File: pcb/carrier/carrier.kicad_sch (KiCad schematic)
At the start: 42 parts, among them J1 Freeze footswitch, J2 Clear footswitch, J3 In L / Mono, J4 In R (normalled from In L), J5 Out L / Mono, J6 Out R (ring = plug detect), SW1 Single / Multi, SW2 +5 up / down, U1 Daisy Seed

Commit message: Carrier board: routed, DRC clean, fab outputs
route_pcb.py sets design rules, autoroutes with Freerouting (retrying
until complete), imports the session file, and pours AGND on both
layers; DRC reports 0 violations and 0 unconnected pads. make_fab.py
writes Gerbers, drill files, a zip, and JLC-style BOM and placement
files for the 21 top-side SMD parts.

Pot mounting tabs are now plated (solderable). The jack footprint is a
project copy with its outline on the fab layer, since the jack noses
overhang the rear edge by design.

Co-Authored-By: Claude Opus 5.5 <noreply@anthropic.com>
Claude-Session: https://claude.ai/code/session_01JAavHVgiwWaG4iqEz4KA1Q
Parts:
- J3, J4, J5, J6: footprint Connector_Audio:Jack_6.35mm_Neutrik_NMJ6HCD2_Horizontal -> carrier:Jack_6.35mm_Neutrik_NMJ6HCD2_Horizontal_FabOnlySilk
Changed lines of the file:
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@@
     (property "Reference" "J3" (at 330 35 0) (effects (font (size 1.27 1.27))))
     (property "Value" "In L / Mono" (at 330 55 0) (effects (font (size 1.27 1.27))))
-    (property "Footprint" "Connector_Audio:Jack_6.35mm_Neutrik_NMJ6HCD2_Horizontal" (at 330 45 0) (effects (font (size 1.27 1.27)) hide))
+    (property "Footprint" "carrier:Jack_6.35mm_Neutrik_NMJ6HCD2_Horizontal_FabOnlySilk" (at 330 45 0) (effects (font (size 1.27 1.27)) hide))
     (property "Datasheet" "" (at 330 45 0) (effects (font (size 1.27 1.27)) hide))
     (property "MPN" "Neutrik NMJ6HCD2" (at 330 45 0) (effects (font (size 1.27 1.27)) hide))
@@
     (property "Reference" "J4" (at 330 73 0) (effects (font (size 1.27 1.27))))
     (property "Value" "In R (normalled from In L)" (at 330 93 0) (effects (font (size 1.27 1.27))))
-    (property "Footprint" "Connector_Audio:Jack_6.35mm_Neutrik_NMJ6HCD2_Horizontal" (at 330 83 0) (effects (font (size 1.27 1.27)) hide))
+    (property "Footprint" "carrier:Jack_6.35mm_Neutrik_NMJ6HCD2_Horizontal_FabOnlySilk" (at 330 83 0) (effects (font (size 1.27 1.27)) hide))
     (property "Datasheet" "" (at 330 83 0) (effects (font (size 1.27 1.27)) hide))
     (property "MPN" "Neutrik NMJ6HCD2" (at 330 83 0) (effects (font (size 1.27 1.27)) hide))
@@
     (property "Reference" "J5" (at 330 111 0) (effects (font (size 1.27 1.27))))
     (property "Value" "Out L / Mono" (at 330 131 0) (effects (font (size 1.27 1.27))))
-    (property "Footprint" "Connector_Audio:Jack_6.35mm_Neutrik_NMJ6HCD2_Horizontal" (at 330 121 0) (effects (font (size 1.27 1.27)) hide))
+    (property "Footprint" "carrier:Jack_6.35mm_Neutrik_NMJ6HCD2_Horizontal_FabOnlySilk" (at 330 121 0) (effects (font (size 1.27 1.27)) hide))
     (property "Datasheet" "" (at 330 121 0) (effects (font (size 1.27 1.27)) hide))
     (property "MPN" "Neutrik NMJ6HCD2" (at 330 121 0) (effects (font (size 1.27 1.27)) hide))
@@
     (property "Reference" "J6" (at 330 149 0) (effects (font (size 1.27 1.27))))
     (property "Value" "Out R (ring = plug detect)" (at 330 169 0) (effects (font (size 1.27 1.27))))
-    (property "Footprint" "Connector_Audio:Jack_6.35mm_Neutrik_NMJ6HCD2_Horizontal" (at 330 159 0) (effects (font (size 1.27 1.27)) hide))
+    (property "Footprint" "carrier:Jack_6.35mm_Neutrik_NMJ6HCD2_Horizontal_FabOnlySilk" (at 330 159 0) (effects (font (size 1.27 1.27)) hide))
     (property "Datasheet" "" (at 330 159 0) (effects (font (size 1.27 1.27)) hide))
     (property "MPN" "Neutrik NMJ6HCD2" (at 330 159 0) (effects (font (size 1.27 1.27)) hide))

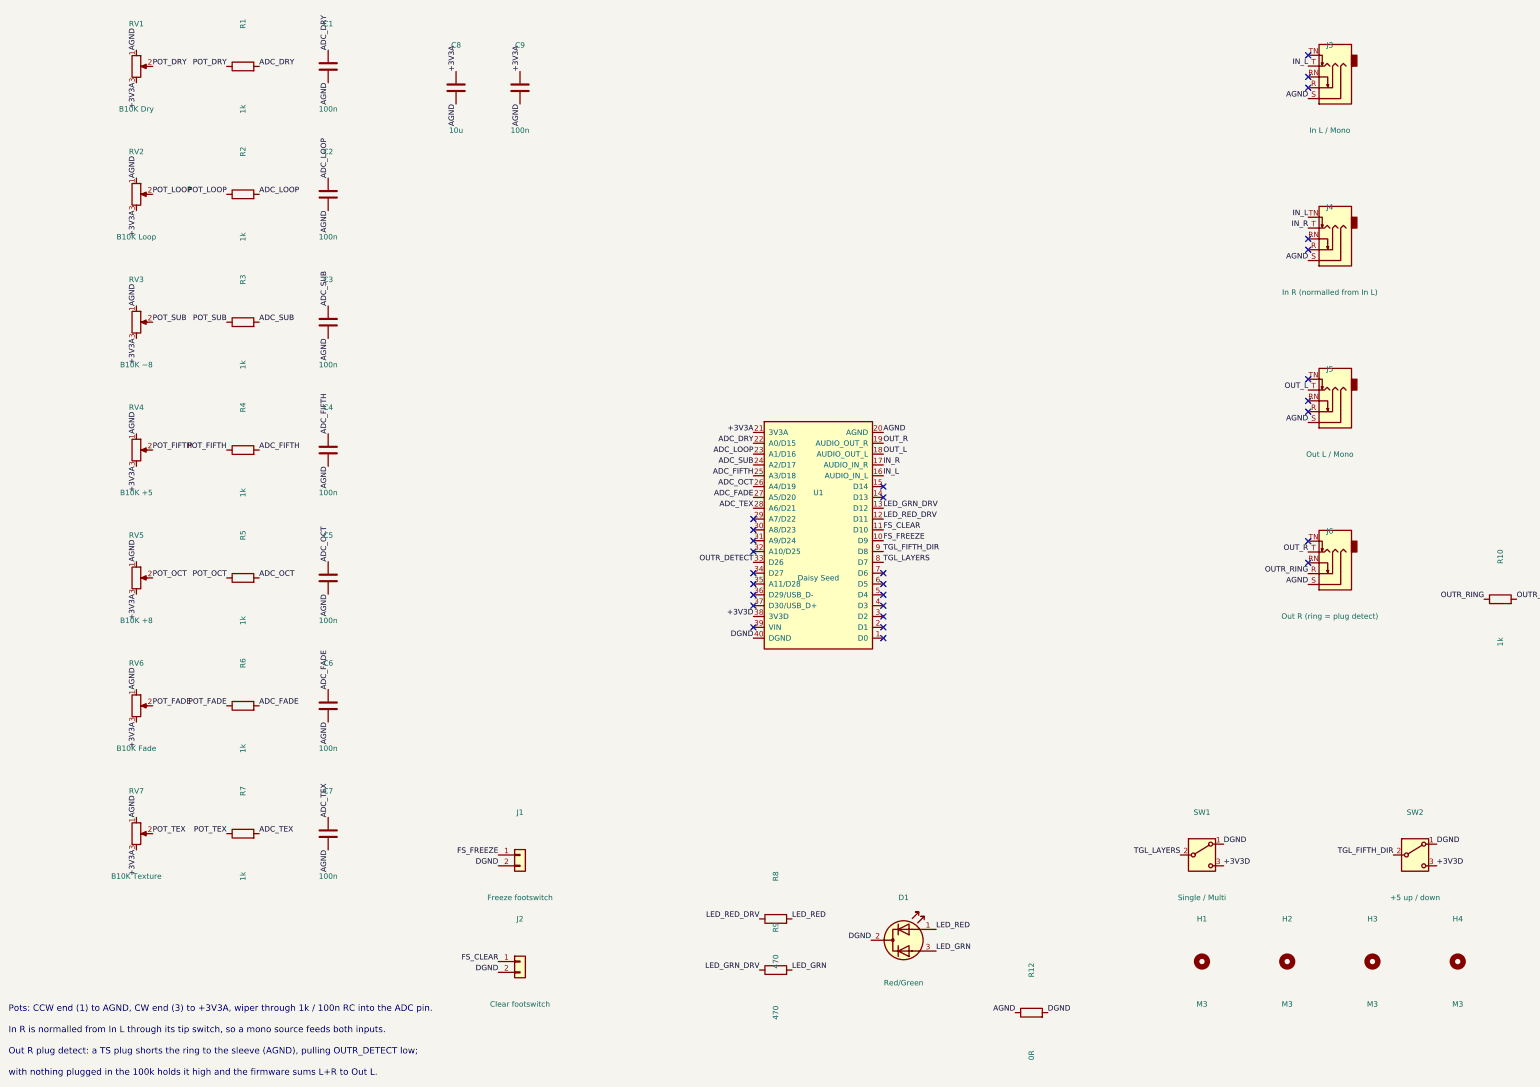
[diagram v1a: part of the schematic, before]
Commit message: Carrier: single ground pour, verified parts
AGND and DGND now tie to one carrier ground (R12 removed), poured on both
layers and stitched with a via grid; re-routed, DRC 0 violations and 0
unconnected. SMD parts carry manufacturer part numbers checked against
their JLC part pages. README records the jack panel-thickness check
(NMJ6HCD2 is rated under 4.7 mm) and the placement-rotation note.

Co-Authored-By: Claude Opus 5.5 <noreply@anthropic.com>
Claude-Session: https://claude.ai/code/session_01JAavHVgiwWaG4iqEz4KA1Q
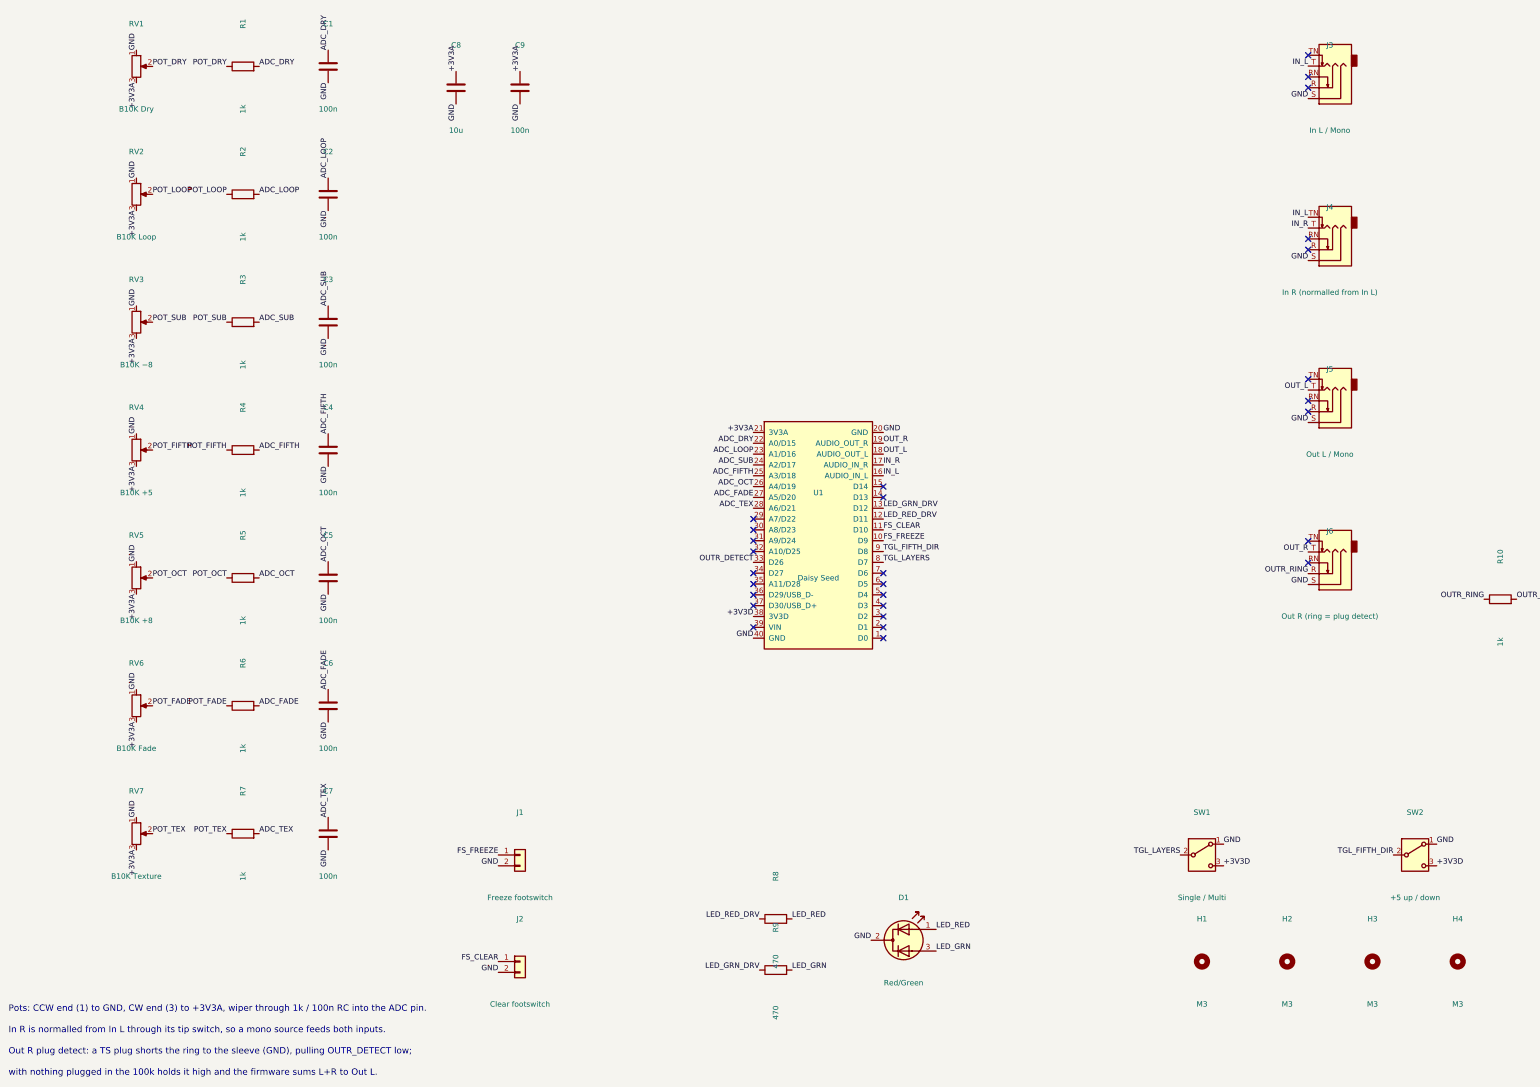
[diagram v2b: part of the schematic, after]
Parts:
- removed R12: 0R, Resistor_SMD:R_0603_1608Metric, symbol Device:R
- C1, C2, C3, C4, C5, C6, C7, C9: MPN (none) -> YAGEO CC0603KRX7R9BB104
- C8: MPN (none) -> Samsung CL21A106KAYNNNE (25 V X5R)
- R1, R10, R2, R3, R4, R5, R6, R7: MPN (none) -> UNI-ROYAL 0603WAF1001T5E
- R11: MPN (none) -> UNI-ROYAL 0603WAF1003T5E
- R8, R9: MPN (none) -> UNI-ROYAL 0603WAF4700T5E
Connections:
- net DGND is gone; now on net GND: D1.2 (K), J1.2 (Pin_2), J2.2 (Pin_2), SW1.1 (A), SW2.1 (A), U1.40 (GND)
- net AGND renamed GND
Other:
- note added: "Out R plug detect: a TS plug shorts the ring to the sleeve (GND), pulling OUTR_DETECT low;"
- note added: "Pots: CCW end (1) to GND, CW end (3) to +3V3A, wiper through 1k / 100n RC into the ADC pin."
- note removed: "Out R plug detect: a TS plug shorts the ring to the sleeve (AGND), pulling OUTR_DETECT low;"
- note removed: "Pots: CCW end (1) to AGND, CW end (3) to +3V3A, wiper through 1k / 100n RC into the ADC pin."

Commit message: Apply design review fixes (Seed3 target)
Mechanical (from datasheets):
- Jack axis is 7.53 mm off the PCB (NMJ6HCD2: 15.67 body, axis 8.14
  below its top), not 9.1; back-wall slots moved.
- Toggle bushing base is 10.39 mm above the PCB (E-Switch catalog p.2
  body 8.89 + 1.5 mm M2 pin standoff), so the carrier now hangs 10.39 mm
  under the panel; pots move to 25 mm shafts (11.1 mm above the panel),
  toggles get 5.4 mm of thread for the nut.
- Seed3 geometry: 18 mm wide, 2.5 mm header spacer, USB-C axis 14.2 mm
  below the carrier; USB slot widened to 14 x 9 mm.
- LED sits on a 5 mm spacer to reach its panel hole.

Electrical:
- Out R plug detect now uses the ring-normal contact with the ring
  grounded, so TS and TRS plugs are both detected.
- In L's tip-normal grounds the input when nothing is plugged in.
- 10 uF series + 100 k bleed on each output, per the Seed3 reference.
- Input pad footprints per channel, fitted as no pad (0R, shunt DNP).

Re-routed: DRC 0 violations, 0 unconnected. BOM excludes DNP parts.

Co-Authored-By: Claude Opus 5.5 <noreply@anthropic.com>
Claude-Session: https://claude.ai/code/session_01JAavHVgiwWaG4iqEz4KA1Q
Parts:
- added C10, C11: 10u, Capacitor_SMD:C_0805_2012Metric, symbol Device:C
- added R13, R14: 100k, Resistor_SMD:R_0603_1608Metric, symbol Device:R
- added R15, R17: 0R, Resistor_SMD:R_0603_1608Metric, symbol Device:R
- added R16, R18: DNP 10k, Resistor_SMD:R_0603_1608Metric, symbol Device:R
- J3: value In L / Mono -> In L / Mono (grounded when empty)
- J6: value Out R (ring = plug detect) -> Out R (ring switch = plug detect)
- RV1, RV2, RV3, RV4, RV5, RV6, RV7: MPN Alpha RV09AF-40-20K-B10K -> Alpha RV09AF-40-25K-B10K (25 mm knurled shaft)
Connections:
- net GND: now also J3.TN, J6.R, R13.2, R14.2, R16.2, R18.2
- net IN_L: now also R15.2, R16.1; no longer J3.T, J4.TN
- net IN_R: now also R17.2, R18.1; no longer J4.T
- net OUT_L: now also C10.1; no longer J5.T
- net OUT_R: now also C11.1; no longer J6.T
- net OUTR_SENSE: now reaches J6.RN
- net OUTR_SENSE: now also R10.1
- removed net OUTR_RING: J6.R, R10.1
- new net JIN_L: J3.T, J4.TN, R15.1
- new net JIN_R: J4.T, R17.1
- new net JOUT_L: C10.2, J5.T, R13.1
- new net JOUT_R: C11.2, J6.T, R14.1
- no-connect marks 28 -> 26
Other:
- note added: "In R is normalled from In L's jack tip; In L's tip switch grounds it when nothing is plugged in."
- note added: "Out R plug detect: ring tied to GND, ring-normal contact to OUTR_DETECT. Empty jack: RN touches the ring"
- note added: "spring, so the pin reads low; any plug (TS or TRS) lifts it and the 100k pulls high. Low = sum to Out L."
- note removed: "In R is normalled from In L through its tip switch, so a mono source feeds both inputs."
- note removed: "Out R plug detect: a TS plug shorts the ring to the sleeve (GND), pulling OUTR_DETECT low;"
- note removed: "with nothing plugged in the 100k holds it high and the firmware sums L+R to Out L."

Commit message: Rev B carrier: bare board, all through-hole, mono in / stereo out
Drops fab assembly. The board is all through-hole with six small parts:
two output coupling caps, two bleed resistors, two LED resistors. Pot
RC filters, supply caps, input pads, the In R jack and the plug-detect
resistors are gone (pots straight to the ADCs, Out R detect and switches
on internal pull-ups). Mono input feeds both codec inputs; stereo out
kept. Three jacks on the back wall. Re-routed, DRC 0 violations.
make_fab.py now writes Gerbers plus a hand-solder bom.csv.

Co-Authored-By: Claude Opus 5.5 <noreply@anthropic.com>
Claude-Session: https://claude.ai/code/session_01JAavHVgiwWaG4iqEz4KA1Q
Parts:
- removed C10, C11, C8: 10u, Capacitor_SMD:C_0805_2012Metric, symbol Device:C
- removed C3, C4, C5, C6, C7, C9: 100n, Capacitor_SMD:C_0603_1608Metric, symbol Device:C
- removed J6: Out R (ring switch = plug detect), carrier:Jack_6.35mm_Neutrik_NMJ6HCD2_Horizontal_FabOnlySilk, symbol Connector_Audio:AudioJack3_SwitchTR
- removed R10, R5, R6, R7: 1k, Resistor_SMD:R_0603_1608Metric, symbol Device:R
- removed R11, R13, R14: 100k, Resistor_SMD:R_0603_1608Metric, symbol Device:R
- removed R15, R17: 0R, Resistor_SMD:R_0603_1608Metric, symbol Device:R
- removed R16, R18: DNP 10k, Resistor_SMD:R_0603_1608Metric, symbol Device:R
- removed R8, R9: 470, Resistor_SMD:R_0603_1608Metric, symbol Device:R
- C1, C2: value 100n -> 10u; footprint Capacitor_SMD:C_0603_1608Metric -> Capacitor_THT:C_Disc_D5.0mm_W2.5mm_P5.00mm; LCSC C14663 -> (none); MPN YAGEO CC0603KRX7R9BB104 -> 10 uF 25 V X7R radial MLCC, 5.08 mm leads (e.g. TDK FG28X7R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
- D1: MPN 5 mm bi-colour LED, common cathode (red/green) -> 5 mm bi-colour LED, common cathode (red/green), on a 5 mm s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
- J3: value In L / Mono (grounded when empty) -> In (mono; grounded when empty)
- J4: value In R (normalled from In L) -> Out L / Mono
- J5: value Out L / Mono -> Out R (ring switch = plug detect)
- R1, R2: value 1k -> 470; footprint Resistor_SMD:R_0603_1608Metric -> Resistor_THT:R_Axial_DIN0207_L6.3mm_D2.5mm_P7.62mm_Horizontal; LCSC C21190 -> (none); MPN UNI-ROYAL 0603WAF1001T5E -> 470R 1/4 W (choose per LED)
- R3, R4: value 1k -> 100k; footprint Resistor_SMD:R_0603_1608Metric -> Resistor_THT:R_Axial_DIN0207_L6.3mm_D2.5mm_P7.62mm_Horizontal; LCSC C21190 -> (none); MPN UNI-ROYAL 0603WAF1001T5E -> 100k 1/4 W metal film
- U1: value Daisy Seed -> Daisy Seed3; MPN Electrosmith Daisy Seed (on 2x 1x20 female headers) -> Electrosmith Daisy Seed3 (on 2x 1x20 female headers)
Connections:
- net ADC_FADE is gone; now on net POT_FADE: U1.27 (A5/D20)
- net ADC_OCT is gone; now on net POT_OCT: U1.26 (A4/D19)
- net ADC_TEX is gone; now on net POT_TEX: U1.28 (A6/D21)
- net IN_R is gone; now on net AUDIO_IN: U1.17 (AUDIO_IN_R)
- net JIN_R is gone; now on net JOUT_L: J4.T
- net GND: now also J5.R, R3.2, R4.2; no longer C1.2, C2.2
- net JOUT_L: now also C1.2, R3.1; no longer J5.T
- net JOUT_R: now also C2.2, J5.T, R4.1
- net LED_GRN: now also R2.2
- net LED_GRN_DRV: now also R2.1
- net LED_RED: now also R1.2
- net LED_RED_DRV: now also R1.1
- net OUTR_DETECT: now also J5.RN
- net OUT_L: now also C1.1
- net OUT_R: now also C2.1
- net POT_DRY: now also U1.22 (A0/D15); no longer R1.1
- net POT_FIFTH: now also U1.25 (A3/D18); no longer R4.1
- net POT_LOOP: now also U1.23 (A1/D16); no longer R2.1
- net POT_SUB: now also U1.24 (A2/D17); no longer R3.1
- removed net ADC_DRY: C1.1, R1.2, U1.22 (A0/D15)
- removed net ADC_FIFTH: R4.2, U1.25 (A3/D18)
- removed net ADC_LOOP: C2.1, R2.2, U1.23 (A1/D16)
- removed net ADC_SUB: R3.2, U1.24 (A2/D17)
- net IN_L renamed AUDIO_IN
- net AUDIO_IN: now also J3.T
- net JIN_L: no longer names the net of J4.TN
- net JIN_L: no longer J3.T
- no-connect marks 26 -> 24
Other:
- note added: "Mono in feeds both codec inputs; the In jack's tip switch grounds the input when nothing is plugged in."
- note added: "Out R plug detect: ring tied to GND, ring-normal contact to D26 (internal pull-up). Empty jack reads low,"
- note added: "Pots: CCW end (1) to GND, CW end (3) to +3V3A, wiper straight to the ADC pin; firmware smooths readings."
- note added: "any plug reads high. Low = firmware sums to Out L. Toggles and footswitches use no resistors."
- note removed: "In R is normalled from In L's jack tip; In L's tip switch grounds it when nothing is plugged in."
- note removed: "Out R plug detect: ring tied to GND, ring-normal contact to OUTR_DETECT. Empty jack: RN touches the ring"
- note removed: "Pots: CCW end (1) to GND, CW end (3) to +3V3A, wiper through 1k / 100n RC into the ADC pin."
- note removed: "spring, so the pin reads low; any plug (TS or TRS) lifts it and the 100k pulls high. Low = sum to Out L."
- moved on the sheet: C1, C2, J4, J5, R1, R2, R3, R4
